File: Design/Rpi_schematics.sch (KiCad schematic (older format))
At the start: 2 parts

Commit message: added DHT11 and smart doorbell button and led
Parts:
- P?: value CONN_4 -> DHT11
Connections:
- net +3.3V: now also P?.1 (P1)
- net Door Bell LED: now reaches PI?.11 (GPIO17)
- net Door Bell Button: now reaches PI?.18 (GPIO24)
- net Coffermaker: now reaches PI?.7 (GPIO4)
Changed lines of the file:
@@
 LIBS:contrib
 LIBS:valves
-LIBS:Raspberry_PI_B+
 LIBS:Rpi_schematics-cache
-LIBS:raspberry_pi
 EELAYER 27 0
 EELAYER END
@@
 Sheet 1 1
 Title ""
-Date "1 aug 2015"
+Date "9 sep 2015"
 Rev ""
 Comp ""
@@
 P 4350 4050
 F 0 "P?" V 4300 4050 50  0000 C CNN
-F 1 "CONN_4" V 4400 4050 50  0000 C CNN
+F 1 "DHT11" V 4400 4050 50  0000 C CNN
 F 2 "" H 4350 4050 60  0000 C CNN
 F 3 "" H 4350 4050 60  0000 C CNN
@@
 Wire Wire Line
 	5450 4100 5450 4200
+Wire Wire Line
+	4700 3900 4850 3900
+Wire Wire Line
+	4850 3900 4850 3750
+Text GLabel 5150 2700 0    39   Output ~ 0
+Door Bell LED
+Wire Wire Line
+	5500 2700 5150 2700
+Text GLabel 6600 3000 2    39   Output ~ 0
+Door Bell Button
+Wire Wire Line
+	6600 3000 6300 3000
+Text GLabel 5150 2500 0    39   Output ~ 0
+Coffermaker
+Wire Wire Line
+	5150 2500 5500 2500
 $EndSCHEMATC

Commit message: Added closet door button
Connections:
- net +3.3V: now also PI?.1 (3V3)
- net Closet Door Button: now reaches PI?.12 (GPIO18)
- net +5V: now reaches PI?.2 (5V)
- net +5V: now also PI?.4 (5V)
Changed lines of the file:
@@
 Wire Wire Line
 	5150 2500 5500 2500
+$Comp
+L +3,3V #PWR?
+U 1 1 55F08746
+P 5400 2100
+F 0 "#PWR?" H 5400 2060 30  0001 C CNN
+F 1 "+3,3V" H 5400 2210 30  0000 C CNN
+F 2 "" H 5400 2100 60  0000 C CNN
+F 3 "" H 5400 2100 60  0000 C CNN
+	1    5400 2100
+	1    0    0    -1
+$EndComp
+Wire Wire Line
+	5400 2100 5400 2200
+Wire Wire Line
+	5400 2200 5500 2200
+$Comp
+L +5V #PWR?
+U 1 1 55F0876B
+P 6350 2100
+F 0 "#PWR?" H 6350 2190 20  0001 C CNN
+F 1 "+5V" H 6350 2190 30  0000 C CNN
+F 2 "" H 6350 2100 60  0000 C CNN
+F 3 "" H 6350 2100 60  0000 C CNN
+	1    6350 2100
+	1    0    0    -1
+$EndComp
+Wire Wire Line
+	6350 2100 6350 2300
+Wire Wire Line
+	6350 2200 6300 2200
+Wire Wire Line
+	6350 2300 6300 2300
+Connection ~ 6350 2200
+Text GLabel 6600 2700 2    39   Output ~ 0
+Closet Door Button
+Wire Wire Line
+	6600 2700 6300 2700
 $EndSCHEMATC

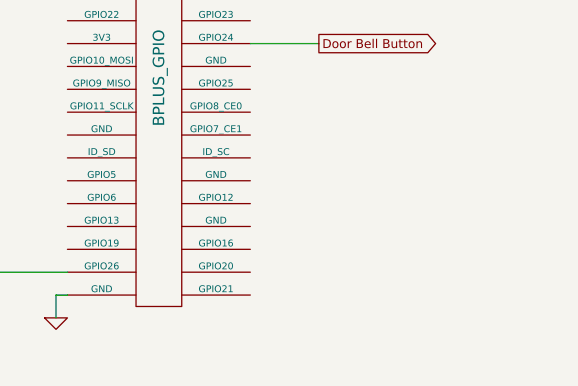
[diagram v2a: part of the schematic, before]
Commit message: added ultrasonic sensor for the smart door bell
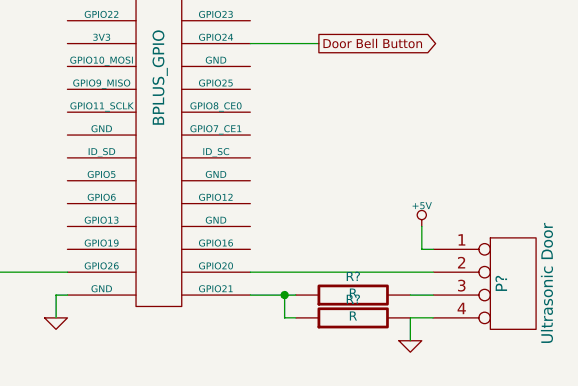
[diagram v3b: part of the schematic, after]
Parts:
- added P?: Ultrasonic Door, symbol CONN_4
- added R? (x2): R, ~, symbol R
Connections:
- net +5V: now also P?.1 (P1)
- net GND: now also P?.4 (P4), R?.2
- net at PI?.38 (GPIO20): now also P?.2 (P2)
- net at PI?.40 (GPIO21): now also R?.1, R?.1
- new net: P?.3 (P3), R?.2
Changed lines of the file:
@@
 Wire Wire Line
 	6600 2700 6300 2700
+$Comp
+L CONN_4 P?
+U 1 1 55F0916F
+P 7450 4050
+F 0 "P?" V 7400 4050 50  0000 C CNN
+F 1 "Ultrasonic Door" V 7600 4050 50  0000 C CNN
+F 2 "" H 7450 4050 60  0000 C CNN
+F 3 "" H 7450 4050 60  0000 C CNN
+	1    7450 4050
+	1    0    0    -1
+$EndComp
+$Comp
+L +5V #PWR?
+U 1 1 55F091B0
+P 7050 3800
+F 0 "#PWR?" H 7050 3890 20  0001 C CNN
+F 1 "+5V" H 7050 3890 30  0000 C CNN
+F 2 "" H 7050 3800 60  0000 C CNN
+F 3 "" H 7050 3800 60  0000 C CNN
+	1    7050 3800
+	1    0    0    -1
+$EndComp
+Wire Wire Line
+	7050 3800 7050 3900
+Wire Wire Line
+	7050 3900 7100 3900
+$Comp
+L GND #PWR?
+U 1 1 55F091D1
+P 7000 4300
+F 0 "#PWR?" H 7000 4300 30  0001 C CNN
+F 1 "GND" H 7000 4230 30  0001 C CNN
+F 2 "" H 7000 4300 60  0000 C CNN
+F 3 "" H 7000 4300 60  0000 C CNN
+	1    7000 4300
+	1    0    0    -1
+$EndComp
+Wire Wire Line
+	7000 4300 7000 4200
+Wire Wire Line
+	7000 4200 7100 4200
+Wire Wire Line
+	7100 4000 6300 4000
+$Comp
+L R R?
+U 1 1 55F09299
+P 6750 4100
+F 0 "R?" V 6830 4100 40  0000 C CNN
+F 1 "R" V 6757 4101 40  0000 C CNN
+F 2 "~" V 6680 4100 30  0000 C CNN
+F 3 "~" H 6750 4100 30  0000 C CNN
+	1    6750 4100
+	0    -1   -1   0
+$EndComp
+$Comp
+L R R?
+U 1 1 55F092B3
+P 6750 4200
+F 0 "R?" V 6830 4200 40  0000 C CNN
+F 1 "R" V 6757 4201 40  0000 C CNN
+F 2 "~" V 6680 4200 30  0000 C CNN
+F 3 "~" H 6750 4200 30  0000 C CNN
+	1    6750 4200
+	0    -1   -1   0
+$EndComp
+Wire Wire Line
+	7000 4100 7100 4100
+Wire Wire Line
+	6500 4100 6300 4100
+Wire Wire Line
+	6500 4200 6450 4200
+Wire Wire Line
+	6450 4200 6450 4100
+Connection ~ 6450 4100
 $EndSCHEMATC

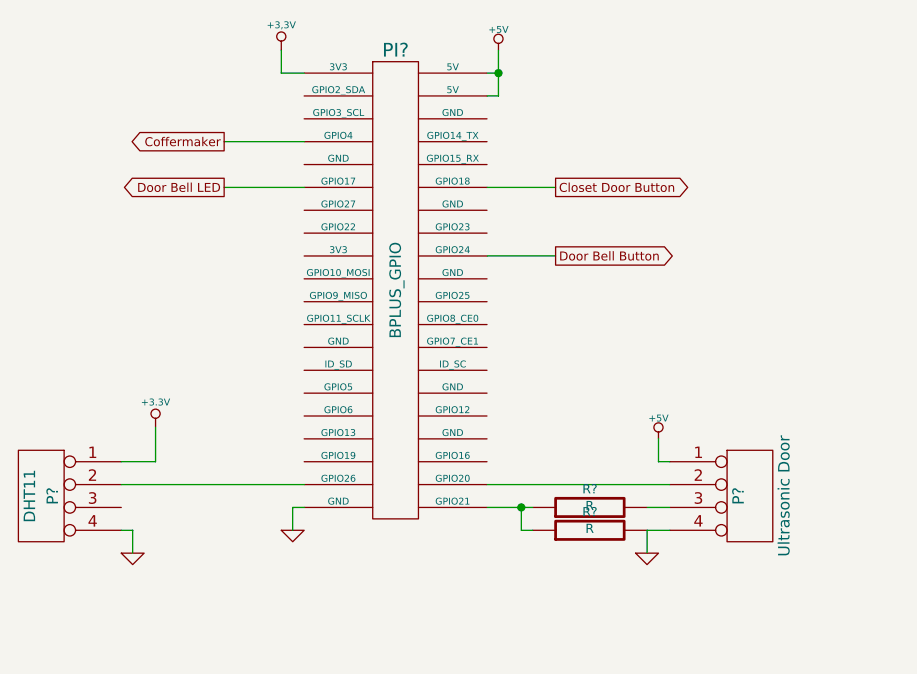
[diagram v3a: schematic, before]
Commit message: Added TV proximity sensor
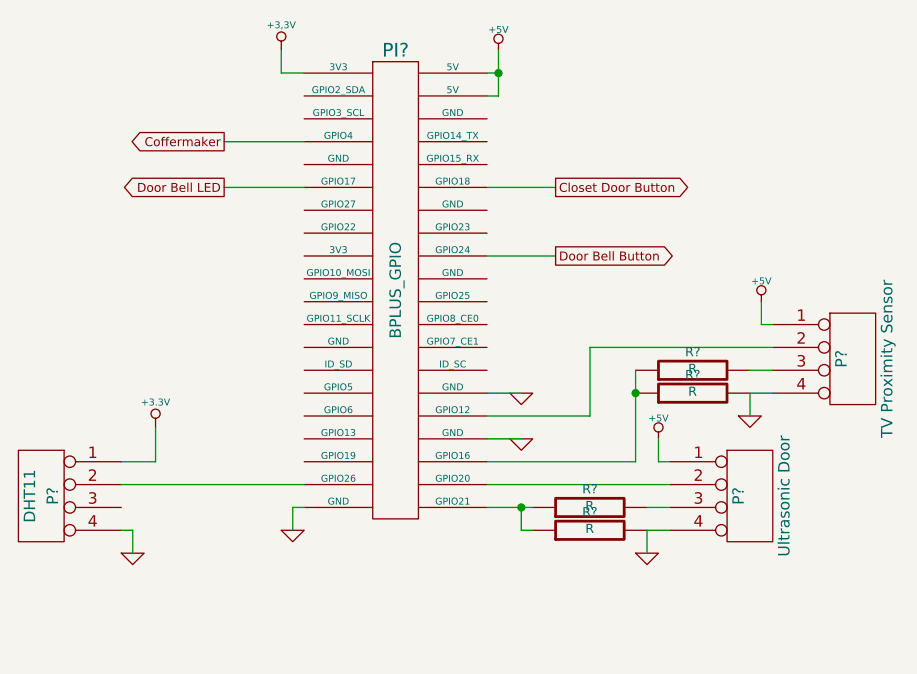
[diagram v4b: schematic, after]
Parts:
- added P?: TV Proximity Sensor, symbol CONN_4
- added R? (x2): R, ~, symbol R
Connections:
- net +5V: now also P?.1 (P1)
- net GND: now also PI?.30 (GND), PI?.34 (GND), P?.4 (P4), R?.2
- net at PI?.32 (GPIO12): now also P?.2 (P2)
- net at PI?.36 (GPIO16): now also R?.1, R?.1
- new net: P?.3 (P3), R?.2
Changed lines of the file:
@@
 	6450 4200 6450 4100
 Connection ~ 6450 4100
+$Comp
+L CONN_4 P?
+U 1 1 55F09595
+P 7900 3450
+F 0 "P?" V 7850 3450 50  0000 C CNN
+F 1 "TV Proximity Sensor" V 8050 3450 50  0000 C CNN
+F 2 "" H 7900 3450 60  0000 C CNN
+F 3 "" H 7900 3450 60  0000 C CNN
+	1    7900 3450
+	1    0    0    -1
+$EndComp
+$Comp
+L +5V #PWR?
+U 1 1 55F0959B
+P 7500 3200
+F 0 "#PWR?" H 7500 3290 20  0001 C CNN
+F 1 "+5V" H 7500 3290 30  0000 C CNN
+F 2 "" H 7500 3200 60  0000 C CNN
+F 3 "" H 7500 3200 60  0000 C CNN
+	1    7500 3200
+	1    0    0    -1
+$EndComp
+Wire Wire Line
+	7500 3200 7500 3300
+Wire Wire Line
+	7500 3300 7550 3300
+$Comp
+L GND #PWR?
+U 1 1 55F095A3
+P 7450 3700
+F 0 "#PWR?" H 7450 3700 30  0001 C CNN
+F 1 "GND" H 7450 3630 30  0001 C CNN
+F 2 "" H 7450 3700 60  0000 C CNN
+F 3 "" H 7450 3700 60  0000 C CNN
+	1    7450 3700
+	1    0    0    -1
+$EndComp
+Wire Wire Line
+	7450 3700 7450 3600
+Wire Wire Line
+	7450 3600 7550 3600
+Wire Wire Line
+	7550 3400 6750 3400
+$Comp
+L R R?
+U 1 1 55F095AC
+P 7200 3500
+F 0 "R?" V 7280 3500 40  0000 C CNN
+F 1 "R" V 7207 3501 40  0000 C CNN
+F 2 "~" V 7130 3500 30  0000 C CNN
+F 3 "~" H 7200 3500 30  0000 C CNN
+	1    7200 3500
+	0    -1   -1   0
+$EndComp
+$Comp
+L R R?
+U 1 1 55F095B2
+P 7200 3600
+F 0 "R?" V 7280 3600 40  0000 C CNN
+F 1 "R" V 7207 3601 40  0000 C CNN
+F 2 "~" V 7130 3600 30  0000 C CNN
+F 3 "~" H 7200 3600 30  0000 C CNN
+	1    7200 3600
+	0    -1   -1   0
+$EndComp
+Wire Wire Line
+	7450 3500 7550 3500
+Connection ~ 6950 3600
+Wire Wire Line
+	6950 3500 6950 3900
+Wire Wire Line
+	6950 3900 6300 3900
+Wire Wire Line
+	6750 3400 6750 3700
+Wire Wire Line
+	6750 3700 6300 3700
+$Comp
+L GND #PWR?
+U 1 1 55F09674
+P 6450 3800
+F 0 "#PWR?" H 6450 3800 30  0001 C CNN
+F 1 "GND" H 6450 3730 30  0001 C CNN
+F 2 "" H 6450 3800 60  0000 C CNN
+F 3 "" H 6450 3800 60  0000 C CNN
+	1    6450 3800
+	1    0    0    -1
+$EndComp
+Wire Wire Line
+	6450 3800 6300 3800
+$Comp
+L GND #PWR?
+U 1 1 55F096A8
+P 6450 3600
+F 0 "#PWR?" H 6450 3600 30  0001 C CNN
+F 1 "GND" H 6450 3530 30  0001 C CNN
+F 2 "" H 6450 3600 60  0000 C CNN
+F 3 "" H 6450 3600 60  0000 C CNN
+	1    6450 3600
+	1    0    0    -1
+$EndComp
+Wire Wire Line
+	6450 3600 6300 3600
 $EndSCHEMATC

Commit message: Added Arduino i2c connection
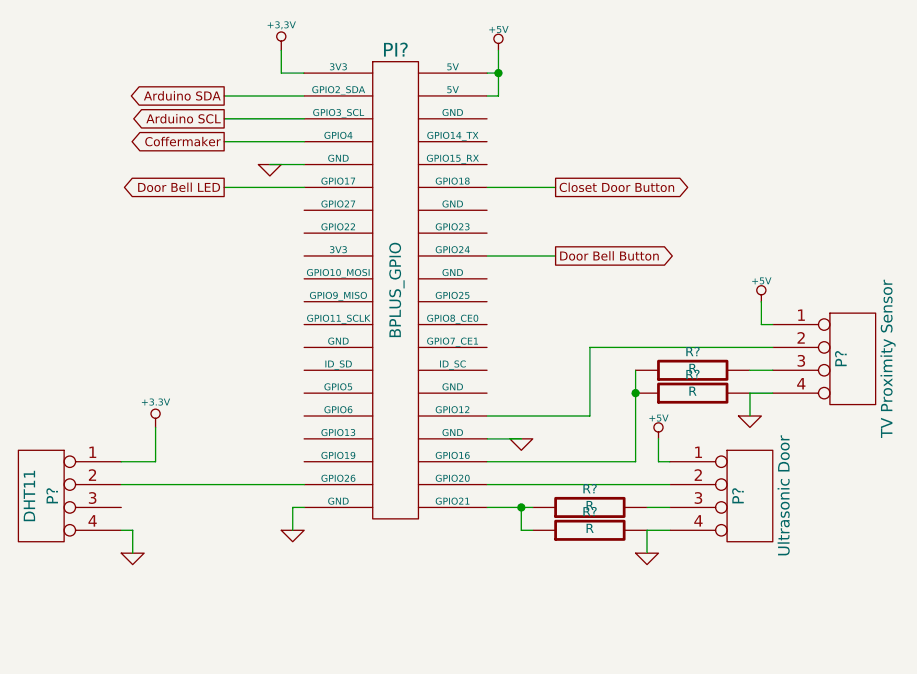
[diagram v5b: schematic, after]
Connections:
- net GND: now also PI?.9 (GND); no longer PI?.30 (GND)
- net Arduino SDA: now reaches PI?.3 (GPIO2_SDA)
- net Arduino SCL: now reaches PI?.5 (GPIO3_SCL)
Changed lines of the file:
@@
 	7000 4100 7100 4100
 Wire Wire Line
-	6500 4100 6300 4100
+	6300 4100 6500 4100
 Wire Wire Line
 	6500 4200 6450 4200
@@
 L GND #PWR?
 U 1 1 55F096A8
-P 6450 3600
-F 0 "#PWR?" H 6450 3600 30  0001 C CNN
-F 1 "GND" H 6450 3530 30  0001 C CNN
-F 2 "" H 6450 3600 60  0000 C CNN
-F 3 "" H 6450 3600 60  0000 C CNN
-	1    6450 3600
+P 5350 2600
+F 0 "#PWR?" H 5350 2600 30  0001 C CNN
+F 1 "GND" H 5350 2530 30  0001 C CNN
+F 2 "" H 5350 2600 60  0000 C CNN
+F 3 "" H 5350 2600 60  0000 C CNN
+	1    5350 2600
 	1    0    0    -1
 $EndComp
+Text GLabel 5150 2300 0    39   Output ~ 0
+Arduino SDA
+Text GLabel 5150 2400 0    39   Output ~ 0
+Arduino SCL
 Wire Wire Line
-	6450 3600 6300 3600
+	5150 2400 5500 2400
+Wire Wire Line
+	5150 2300 5500 2300
+Wire Wire Line
+	5350 2600 5500 2600
 $EndSCHEMATC

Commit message: updated design
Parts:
- added K?: IR, symbol CONN_3
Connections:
- net GND: now also K?.2 (PM)
- net at PI?.35 (GPIO19): now also K?.3 (P3)
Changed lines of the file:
@@
 Sheet 1 1
 Title ""
-Date "9 sep 2015"
+Date "10 nov 2015"
 Rev ""
 Comp ""
@@
 	1    0    0    -1
 $EndComp
-Wire Wire Line
-	4700 4000 5500 4000
 $Comp
 L +3.3V #PWR?
@@
 $Comp
 L GND #PWR?
-U 1 1 55BCDFC1
-P 4750 4300
-F 0 "#PWR?" H 4750 4300 30  0001 C CNN
-F 1 "GND" H 4750 4230 30  0001 C CNN
-F 2 "" H 4750 4300 60  0000 C CNN
-F 3 "" H 4750 4300 60  0000 C CNN
-	1    4750 4300
-	1    0    0    -1
-$EndComp
-$Comp
-L GND #PWR?
 U 1 1 55BCDFD0
-P 5450 4200
-F 0 "#PWR?" H 5450 4200 30  0001 C CNN
-F 1 "GND" H 5450 4130 30  0001 C CNN
-F 2 "" H 5450 4200 60  0000 C CNN
-F 3 "" H 5450 4200 60  0000 C CNN
-	1    5450 4200
-	1    0    0    -1
-$EndComp
-Wire Wire Line
-	4700 4200 4750 4200
-Wire Wire Line
-	4750 4200 4750 4300
-Wire Wire Line
-	5500 4100 5450 4100
-Wire Wire Line
-	5450 4100 5450 4200
-Wire Wire Line
-	4700 3900 4850 3900
-Wire Wire Line
-	4850 3900 4850 3750
+P 5000 4300
+F 0 "#PWR?" H 5000 4300 30  0001 C CNN
+F 1 "GND" H 5000 4230 30  0001 C CNN
+F 2 "" H 5000 4300 60  0000 C CNN
+F 3 "" H 5000 4300 60  0000 C CNN
+	1    5000 4300
+	1    0    0    -1
+$EndComp
 Text GLabel 5150 2700 0    39   Output ~ 0
 Door Bell LED
-Wire Wire Line
-	5500 2700 5150 2700
 Text GLabel 6600 3000 2    39   Output ~ 0
 Door Bell Button
-Wire Wire Line
-	6600 3000 6300 3000
 Text GLabel 5150 2500 0    39   Output ~ 0
 Coffermaker
-Wire Wire Line
-	5150 2500 5500 2500
 $Comp
 L +3,3V #PWR?
@@
 	1    0    0    -1
 $EndComp
-Wire Wire Line
-	5400 2100 5400 2200
-Wire Wire Line
-	5400 2200 5500 2200
 $Comp
 L +5V #PWR?
@@
 	1    0    0    -1
 $EndComp
-Wire Wire Line
-	6350 2100 6350 2300
-Wire Wire Line
-	6350 2200 6300 2200
-Wire Wire Line
-	6350 2300 6300 2300
-Connection ~ 6350 2200
 Text GLabel 6600 2700 2    39   Output ~ 0
 Closet Door Button
-Wire Wire Line
-	6600 2700 6300 2700
 $Comp
 L CONN_4 P?
@@
 	1    0    0    -1
 $EndComp
-Wire Wire Line
-	7050 3800 7050 3900
-Wire Wire Line
-	7050 3900 7100 3900
 $Comp
 L GND #PWR?
@@
 	1    0    0    -1
 $EndComp
-Wire Wire Line
-	7000 4300 7000 4200
-Wire Wire Line
-	7000 4200 7100 4200
-Wire Wire Line
-	7100 4000 6300 4000
 $Comp
 L R R?
@@
 	0    -1   -1   0
 $EndComp
-Wire Wire Line
-	7000 4100 7100 4100
-Wire Wire Line
-	6300 4100 6500 4100
-Wire Wire Line
-	6500 4200 6450 4200
-Wire Wire Line
-	6450 4200 6450 4100
-Connection ~ 6450 4100
 $Comp
 L CONN_4 P?
@@
 	1    0    0    -1
 $EndComp
-Wire Wire Line
-	7500 3200 7500 3300
-Wire Wire Line
-	7500 3300 7550 3300
 $Comp
 L GND #PWR?
@@
 	1    0    0    -1
 $EndComp
-Wire Wire Line
-	7450 3700 7450 3600
-Wire Wire Line
-	7450 3600 7550 3600
-Wire Wire Line
-	7550 3400 6750 3400
 $Comp
 L R R?
@@
 	0    -1   -1   0
 $EndComp
-Wire Wire Line
-	7450 3500 7550 3500
-Connection ~ 6950 3600
-Wire Wire Line
-	6950 3500 6950 3900
-Wire Wire Line
-	6950 3900 6300 3900
-Wire Wire Line
-	6750 3400 6750 3700
-Wire Wire Line
-	6750 3700 6300 3700
 $Comp
 L GND #PWR?
@@
 	1    0    0    -1
 $EndComp
-Wire Wire Line
-	6450 3800 6300 3800
 $Comp
 L GND #PWR?
@@
 Text GLabel 5150 2400 0    39   Output ~ 0
 Arduino SCL
+$Comp
+L CONN_3 K?
+U 1 1 5642521C
+P 4350 3350
+F 0 "K?" V 4300 3350 50  0000 C CNN
+F 1 "IR" V 4400 3350 40  0000 C CNN
+F 2 "" H 4350 3350 60  0000 C CNN
+F 3 "" H 4350 3350 60  0000 C CNN
+	1    4350 3350
+	-1   0    0    -1
+$EndComp
+Wire Wire Line
+	4700 4000 5500 4000
+Wire Wire Line
+	4700 4200 5000 4200
+Wire Wire Line
+	5000 4100 5500 4100
+Wire Wire Line
+	4700 3900 4850 3900
+Wire Wire Line
+	4850 3900 4850 3750
+Wire Wire Line
+	5500 2700 5150 2700
+Wire Wire Line
+	6600 3000 6300 3000
+Wire Wire Line
+	5150 2500 5500 2500
+Wire Wire Line
+	5400 2100 5400 2200
+Wire Wire Line
+	5400 2200 5500 2200
+Wire Wire Line
+	6350 2100 6350 2300
+Wire Wire Line
+	6350 2200 6300 2200
+Wire Wire Line
+	6350 2300 6300 2300
+Connection ~ 6350 2200
+Wire Wire Line
+	6600 2700 6300 2700
+Wire Wire Line
+	7050 3800 7050 3900
+Wire Wire Line
+	7050 3900 7100 3900
+Wire Wire Line
+	7000 4300 7000 4200
+Wire Wire Line
+	7000 4200 7100 4200
+Wire Wire Line
+	7100 4000 6300 4000
+Wire Wire Line
+	7000 4100 7100 4100
+Wire Wire Line
+	6300 4100 6500 4100
+Wire Wire Line
+	6500 4200 6450 4200
+Wire Wire Line
+	6450 4200 6450 4100
+Connection ~ 6450 4100
+Wire Wire Line
+	7500 3200 7500 3300
+Wire Wire Line
+	7500 3300 7550 3300
+Wire Wire Line
+	7450 3700 7450 3600
+Wire Wire Line
+	7450 3600 7550 3600
+Wire Wire Line
+	7550 3400 6750 3400
+Wire Wire Line
+	7450 3500 7550 3500
+Connection ~ 6950 3600
+Wire Wire Line
+	6950 3500 6950 3900
+Wire Wire Line
+	6950 3900 6300 3900
+Wire Wire Line
+	6750 3400 6750 3700
+Wire Wire Line
+	6750 3700 6300 3700
+Wire Wire Line
+	6450 3800 6300 3800
 Wire Wire Line
 	5150 2400 5500 2400
@@
 Wire Wire Line
 	5350 2600 5500 2600
+Wire Wire Line
+	4950 3900 5500 3900
+Wire Wire Line
+	4800 3250 4700 3250
+Wire Wire Line
+	4800 3050 4800 3250
+Wire Wire Line
+	4950 3900 4950 3450
+Wire Wire Line
+	4950 3450 4700 3450
+Wire Wire Line
+	4700 3350 5000 3350
+$Comp
+L +3.3V #PWR?
+U 1 1 56425445
+P 4800 3100
+F 0 "#PWR?" H 4800 3060 30  0001 C CNN
+F 1 "+3.3V" H 4800 3210 30  0000 C CNN
+F 2 "" H 4800 3100 60  0000 C CNN
+F 3 "" H 4800 3100 60  0000 C CNN
+	1    4800 3100
+	1    0    0    -1
+$EndComp
+Wire Wire Line
+	5000 3350 5000 4300
+Connection ~ 5000 4200
+Connection ~ 5000 4100
 $EndSCHEMATC

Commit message: more changes
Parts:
- added R?: 10, ~, symbol R
- R1: renamed from R?; value R -> 4.7k
- R10: renamed from R?; value R -> 10
- R?: value R -> 4.7k
- R?: value R -> 10k
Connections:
- net GND: now also R?.2
- net at P?.2 (P2), PI?.37 (GPIO26): now also R?.1
- net Arduino SCL: no longer names the net of PI?.5 (GPIO3_SCL)
- net Arduino SDA: no longer names the net of PI?.3 (GPIO2_SDA)
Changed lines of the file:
@@
 Sheet 1 1
 Title ""
-Date "10 nov 2015"
+Date "12 jan 2016"
 Rev ""
 Comp ""
@@
 L GND #PWR?
 U 1 1 55BCDFD0
-P 5000 4300
-F 0 "#PWR?" H 5000 4300 30  0001 C CNN
-F 1 "GND" H 5000 4230 30  0001 C CNN
-F 2 "" H 5000 4300 60  0000 C CNN
-F 3 "" H 5000 4300 60  0000 C CNN
-	1    5000 4300
+P 4850 4700
+F 0 "#PWR?" H 4850 4700 30  0001 C CNN
+F 1 "GND" H 4850 4630 30  0001 C CNN
+F 2 "" H 4850 4700 60  0000 C CNN
+F 3 "" H 4850 4700 60  0000 C CNN
+	1    4850 4700
 	1    0    0    -1
 $EndComp
@@
 $EndComp
 $Comp
-L R R?
+L R R1
 U 1 1 55F09299
 P 6750 4100
-F 0 "R?" V 6830 4100 40  0000 C CNN
-F 1 "R" V 6757 4101 40  0000 C CNN
+F 0 "R1" V 6830 4100 40  0000 C CNN
+F 1 "4.7k" V 6757 4101 40  0000 C CNN
 F 2 "~" V 6680 4100 30  0000 C CNN
 F 3 "~" H 6750 4100 30  0000 C CNN
@@
 $EndComp
 $Comp
-L R R?
+L R R10
 U 1 1 55F092B3
 P 6750 4200
-F 0 "R?" V 6830 4200 40  0000 C CNN
-F 1 "R" V 6757 4201 40  0000 C CNN
+F 0 "R10" V 6830 4200 40  0000 C CNN
+F 1 "10" V 6757 4201 40  0000 C CNN
 F 2 "~" V 6680 4200 30  0000 C CNN
 F 3 "~" H 6750 4200 30  0000 C CNN
@@
 P 7200 3500
 F 0 "R?" V 7280 3500 40  0000 C CNN
-F 1 "R" V 7207 3501 40  0000 C CNN
+F 1 "4.7k" V 7207 3501 40  0000 C CNN
 F 2 "~" V 7130 3500 30  0000 C CNN
 F 3 "~" H 7200 3500 30  0000 C CNN
@@
 P 7200 3600
 F 0 "R?" V 7280 3600 40  0000 C CNN
-F 1 "R" V 7207 3601 40  0000 C CNN
+F 1 "10k" V 7207 3601 40  0000 C CNN
 F 2 "~" V 7130 3600 30  0000 C CNN
 F 3 "~" H 7200 3600 30  0000 C CNN
@@
 	1    0    0    -1
 $EndComp
-Text GLabel 5150 2300 0    39   Output ~ 0
-Arduino SDA
-Text GLabel 5150 2400 0    39   Output ~ 0
-Arduino SCL
 $Comp
 L CONN_3 K?
@@
 	4700 4000 5500 4000
 Wire Wire Line
-	4700 4200 5000 4200
-Wire Wire Line
 	5000 4100 5500 4100
 Wire Wire Line
@@
 Wire Wire Line
 	6450 3800 6300 3800
-Wire Wire Line
-	5150 2400 5500 2400
-Wire Wire Line
-	5150 2300 5500 2300
 Wire Wire Line
 	5350 2600 5500 2600
@@
 $EndComp
 Wire Wire Line
-	5000 3350 5000 4300
+	5000 3350 5000 4600
 Connection ~ 5000 4200
 Connection ~ 5000 4100
+$Comp
+L R R?
+U 1 1 56956FC4
+P 4850 4250
+F 0 "R?" V 4930 4250 40  0000 C CNN
+F 1 "10" V 4857 4251 40  0000 C CNN
+F 2 "~" V 4780 4250 30  0000 C CNN
+F 3 "~" H 4850 4250 30  0000 C CNN
+	1    4850 4250
+	1    0    0    -1
+$EndComp
+Wire Wire Line
+	4850 4500 4850 4700
+Wire Wire Line
+	5000 4600 4700 4600
+Connection ~ 4850 4600
+Wire Wire Line
+	4700 4600 4700 4200
+Connection ~ 4850 4000
 $EndSCHEMATC

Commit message: Deleted few files and more fixes
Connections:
- net at PI?.35 (GPIO19): no longer K?.3 (P3)
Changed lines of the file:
@@
 Sheet 1 1
 Title ""
-Date "12 jan 2016"
+Date "22 apr 2016"
 Rev ""
 Comp ""
@@
 	5350 2600 5500 2600
 Wire Wire Line
-	4950 3900 5500 3900
-Wire Wire Line
 	4800 3250 4700 3250
 Wire Wire Line
 	4800 3050 4800 3250
 Wire Wire Line
-	4950 3900 4950 3450
-Wire Wire Line
-	4950 3450 4700 3450
-Wire Wire Line
 	4700 3350 5000 3350
